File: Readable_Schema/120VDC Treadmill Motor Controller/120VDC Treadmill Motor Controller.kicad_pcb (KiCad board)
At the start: 4 copper layers, 186.8 x 133.2 mm, 141 parts, among them J1 TB005-762-03BE, J2 OSTT7020150, J3 TB0011-350-08BE, J4 TB0011-350-08BE, J5 TB0011-350-08BE, J6 TB0011-350-03BE, J7 OSTT7020150, J9 OSTT7020150, K1 T9GV1L14-24, Q1 IPP60R060P7XKSA1, Q2 IPP60R060P7XKSA1, Q3 IPP60R060P7XKSA1, Q4 IPP60R060P7XKSA1, Q5 IPP60R060P7XKSA1, Q7 DN2450N8-G, Q8 VOM1271T, U1 UCC21530DWKR, U2 UCC21530DWKR, U3 TMCS1126B42QDVGRQ1, U4 SN74HCS08DYYR, U5 TPSI3050QDWZRQ1, U6 AMC1311BDWVR

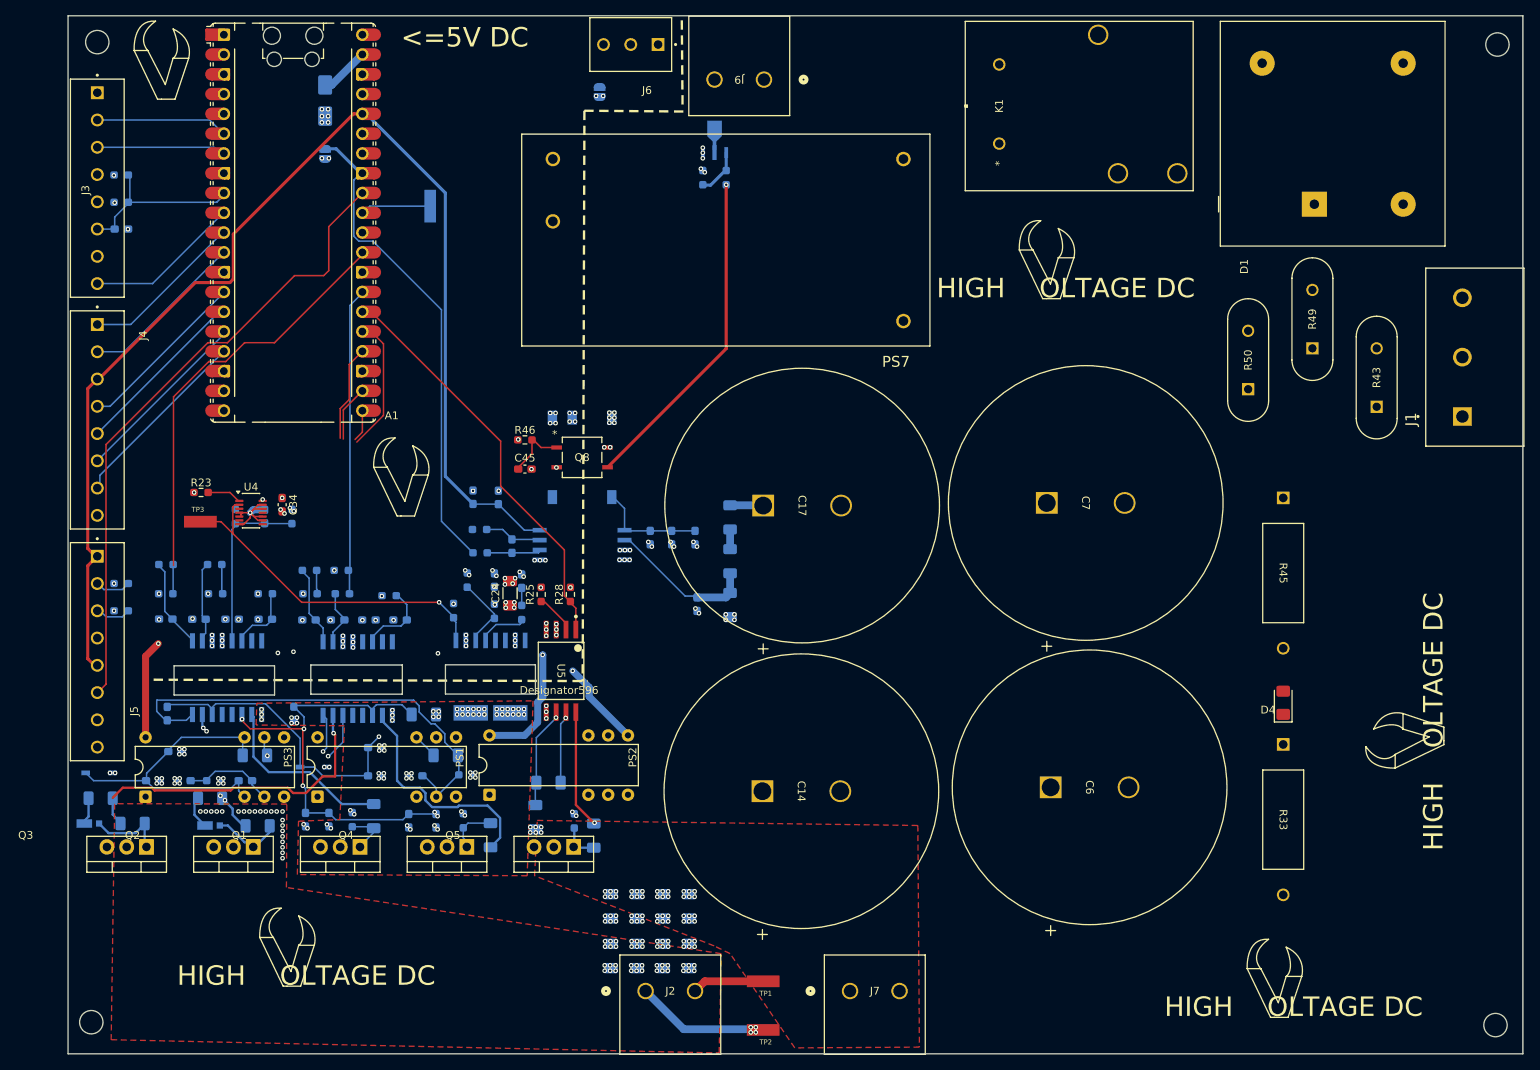
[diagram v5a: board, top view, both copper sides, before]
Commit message: Finished connecting all traces (except for the cap discharge fet which has a pad issue,
-Starting to rip through DRC

-Need to clean up most board fills and make sure things look relatively nice
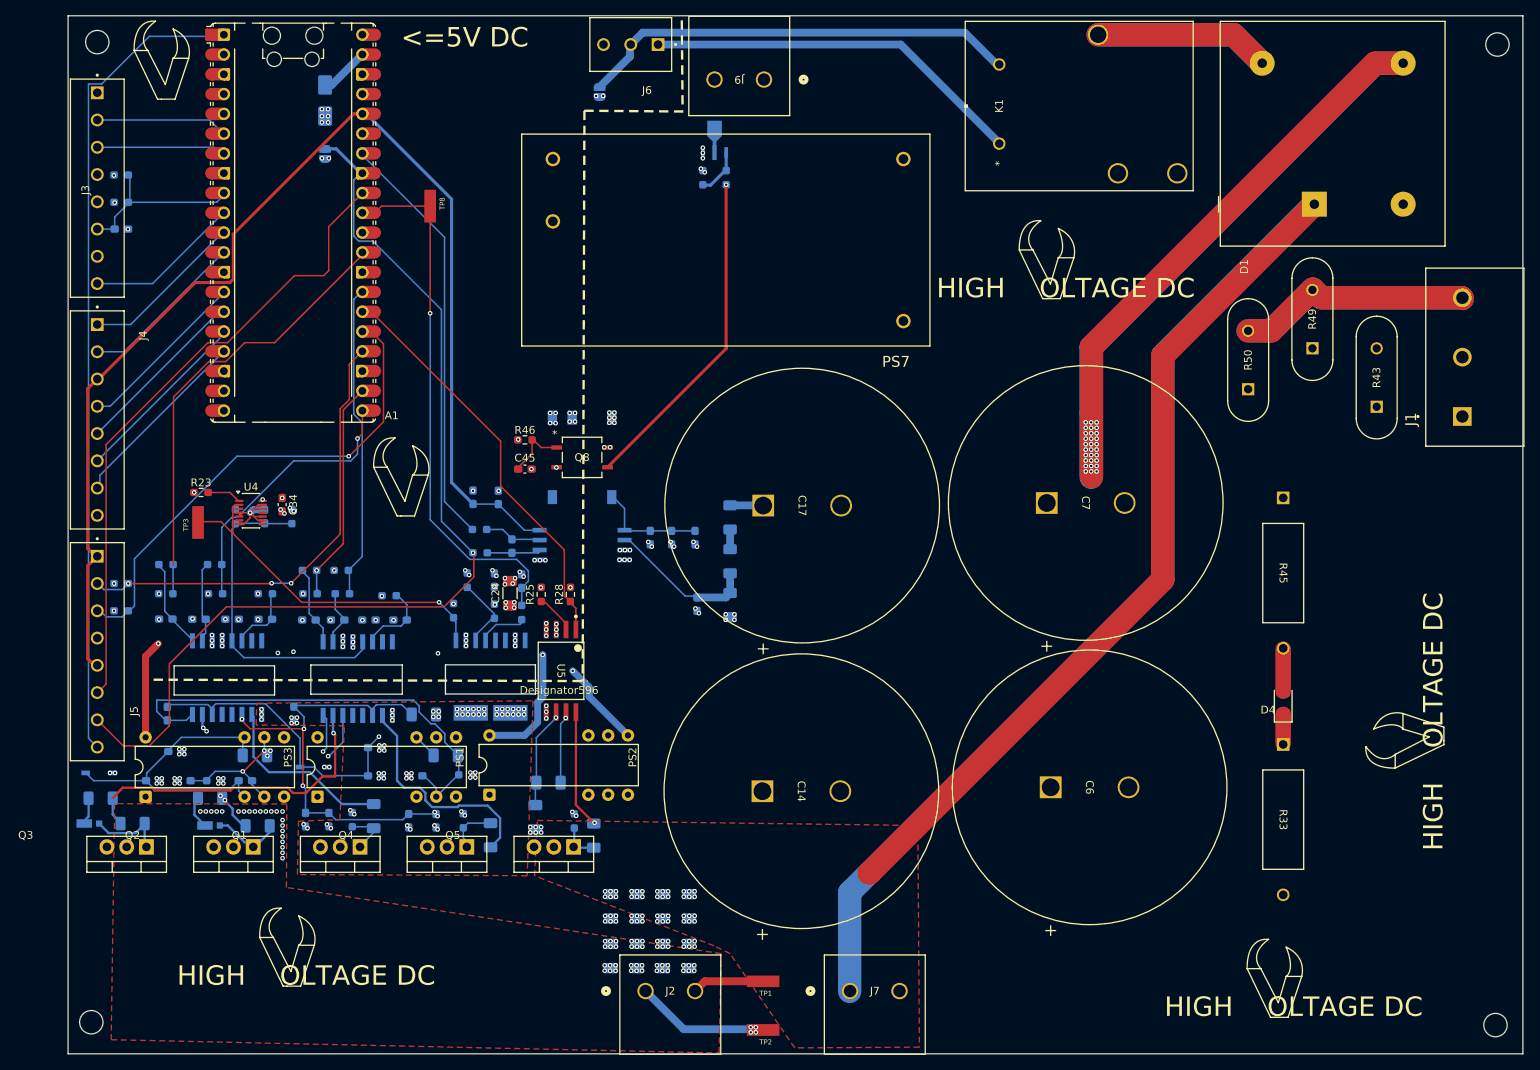
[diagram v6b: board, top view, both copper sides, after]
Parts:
- TP8: moved to F.Cu
- moved TP3 0.32 mm to (33.2, 110.8), turned to 90 degrees
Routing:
- net Net-(D1-+): track 0.00 -> 235.3 mm
- net HV_GND: track 0.00 -> 143.6 mm, vias 99 -> 129
- net /Pi Pico/GP0: track 0.00 -> 105.5 mm
- net /Feedback/adc_gnd: track 61.8 -> 128.3 mm, vias 0 -> 1
- net Net-(J1-Pin_3): track 0.00 -> 60.4 mm
- net /Feedback/v_out: track 11.4 -> 67.9 mm, vias 0 -> 1
- net Net-(J6-Pin_2): track 0.00 -> 56.2 mm
- net /Feedback/cap_vsense: track 0.00 -> 53.8 mm
- net Net-(J6-Pin_1): track 0.00 -> 49.1 mm
- net Net-(D1-Pad2): track 0.00 -> 45.1 mm
- net Net-(A1-GPIO19): track 21.3 -> 63.5 mm, vias 0 -> 1
- net Net-(A1-GPIO18): track 16.6 -> 58.7 mm, vias 0 -> 3
- net /H_Bridge/dir_b: track 7.75 -> 35.4 mm, vias 0 -> 1
- net /H_Bridge/EN_drive: track 21.9 -> 41.0 mm
- net /H_Bridge/pwm_b: track 10.1 -> 28.5 mm, vias 0 -> 1
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- added copper zone on In2.Cu, net /Power/L
- added copper zone on In1.Cu, net /Power/N

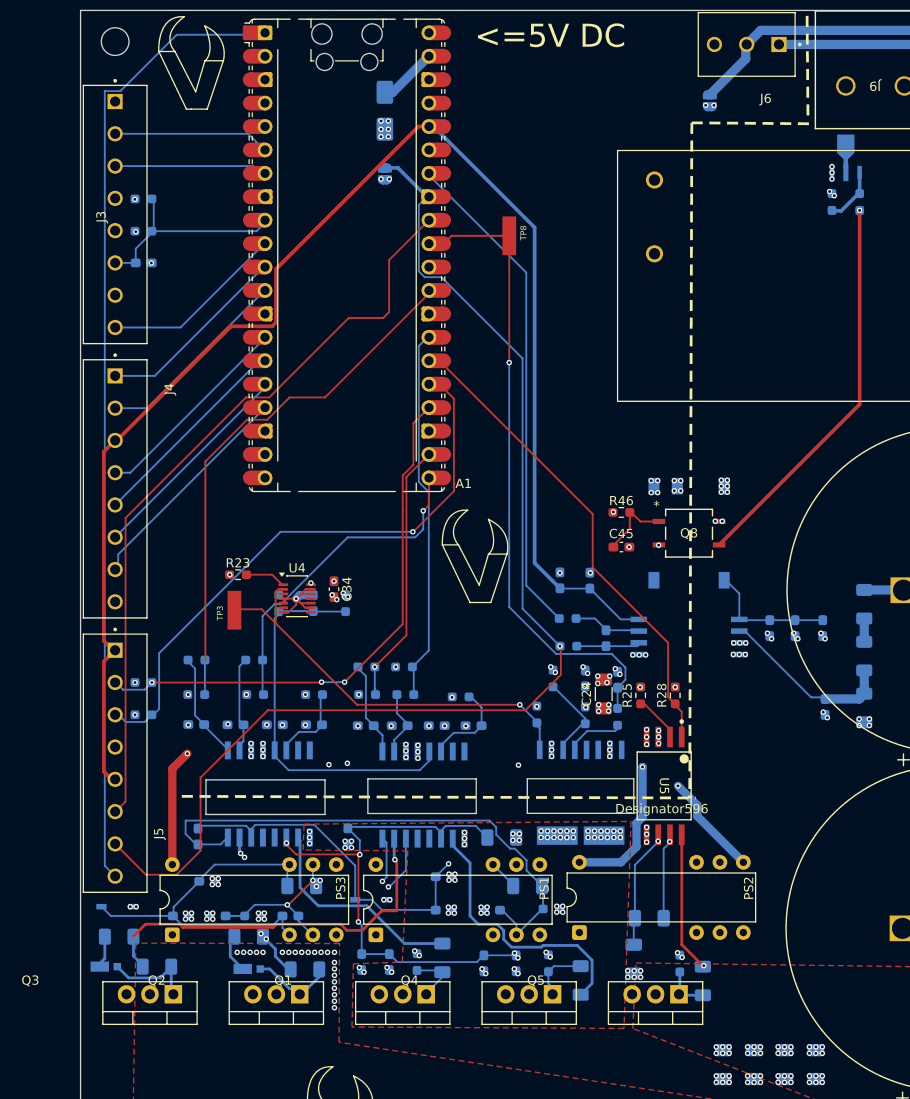
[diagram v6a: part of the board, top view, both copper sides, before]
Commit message: Fixed some smd pad issues with one of the smaller mosfets.
-Need to switch back to low on resistance 250v fets to allow for a smaller heatsink
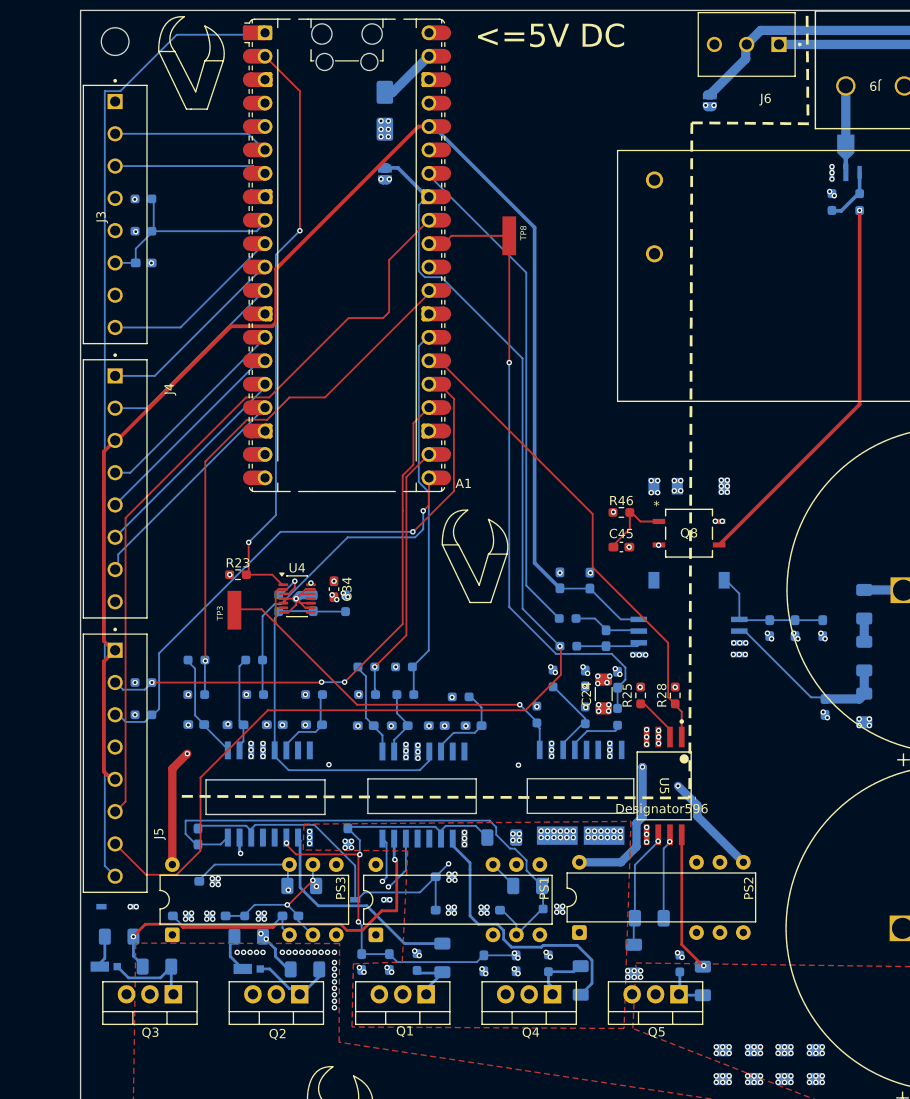
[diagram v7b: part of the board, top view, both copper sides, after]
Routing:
- net /Feedback/mcu_en: track 4.28 -> 64.4 mm, vias 0 -> 2
- net /H_Bridge/hs_ps_2_-: track 58.6 -> 45.0 mm, vias 1 -> 2
- net Net-(J9-Pin_2): track 0.00 -> 5.92 mm
- net /Feedback/EN_Drives: track 0.00 -> 4.30 mm, vias 0 -> 1
- net Net-(Q1-G): track 5.41 -> 6.38 mm
- net /H_Bridge/hs_ps_1_-: track 45.0 -> 45.7 mm
- net Net-(U2-OUTA): vias 4 -> 3
- net Net-(U1-OUTA): vias 1 -> 2
- net 5v 15w: vias 40 -> 39
- net /H_Bridge/pwm_a: vias 0 -> 1
- net /H_Bridge/hs_ps_2_+: vias 5 -> 4

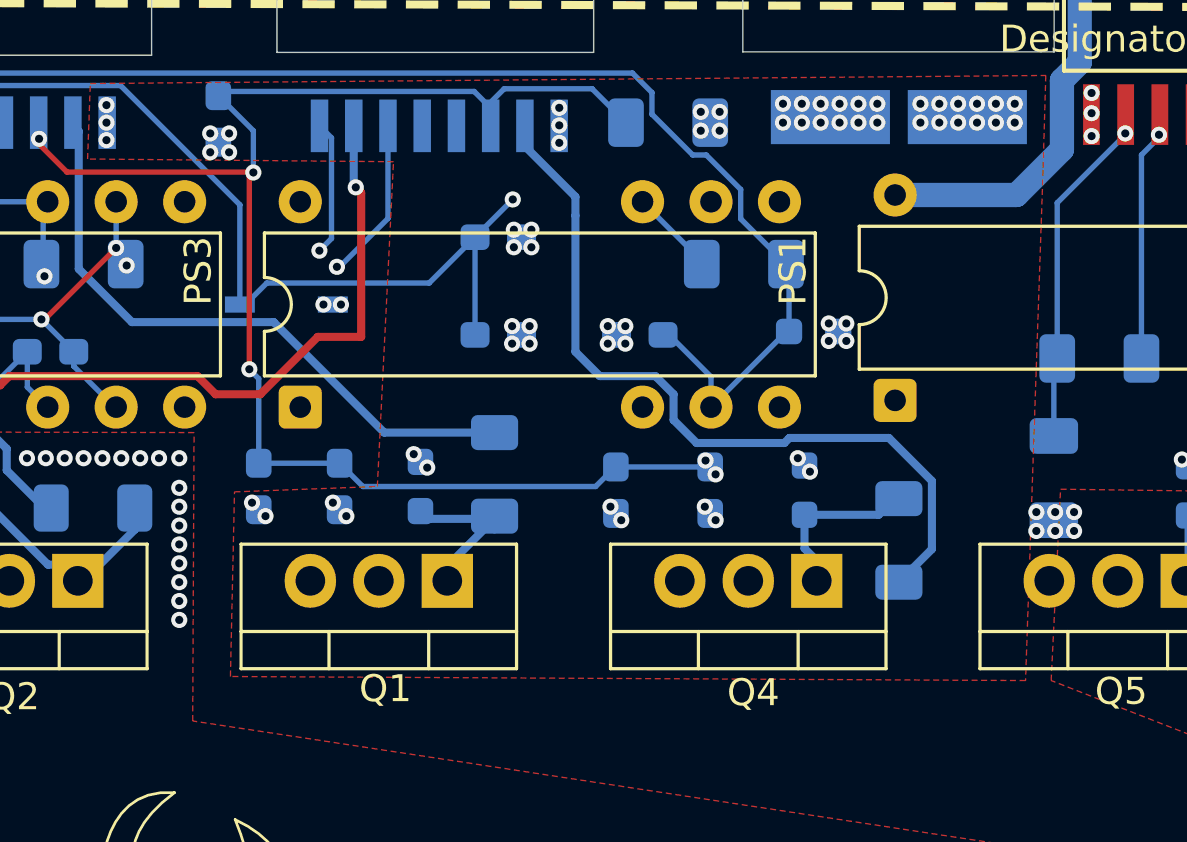
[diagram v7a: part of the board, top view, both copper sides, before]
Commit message: Need to check fet, caps, connector footprints (and cap discharge) on power subcircuit. Currently working through checking all footprints to hopefully save a major headache if there is a mistake
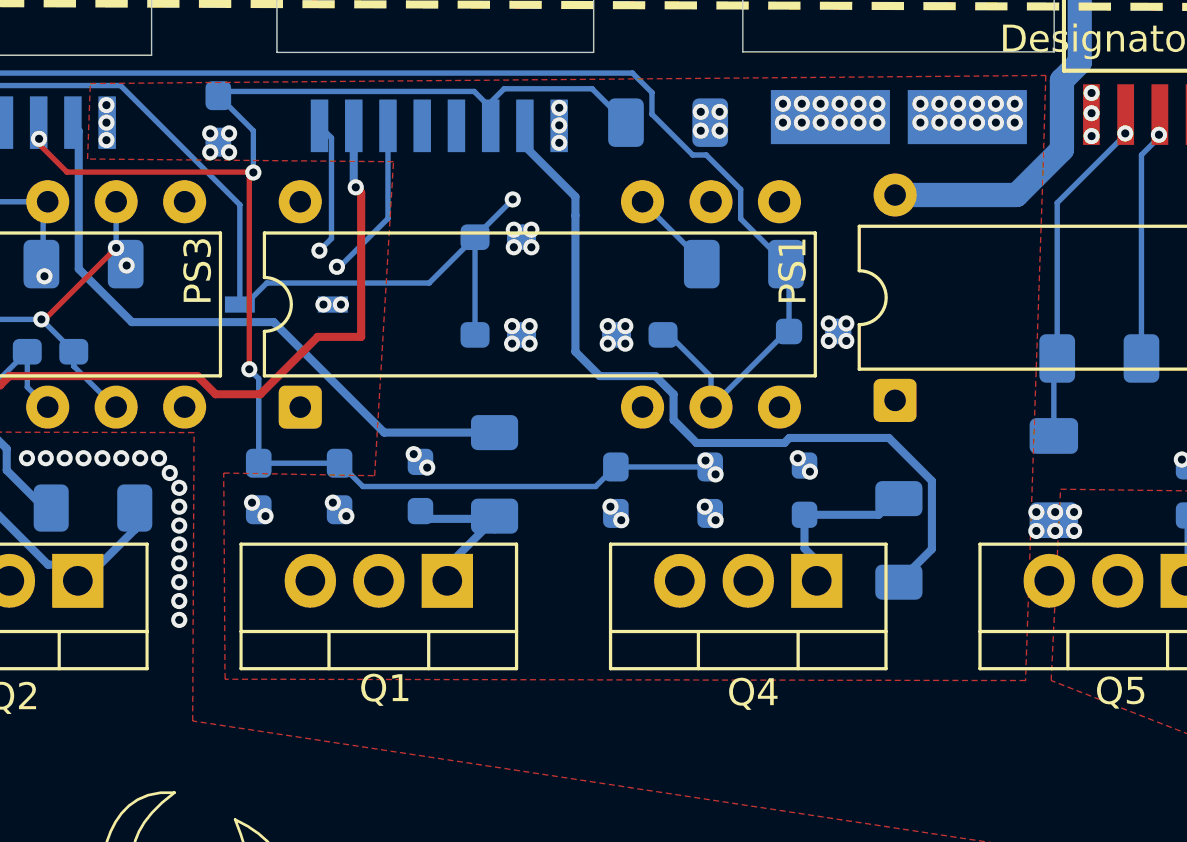
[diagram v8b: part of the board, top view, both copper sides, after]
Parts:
- Q1, Q2, Q3, Q4: value IPP60R060P7XKSA1 -> IPP200N25N3 G
